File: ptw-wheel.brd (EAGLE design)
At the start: 54 x 45 mm, 4 parts

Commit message: Replace GND to N$1 ?
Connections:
- net GND renamed N$1
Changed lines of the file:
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@@
 </elements>
 <signals>
-<signal name="GND">
-<contactref element="U$1" pad="GND"/>
-<contactref element="USB1" pad="GND"/>
-<contactref element="USB1" pad="SHIELD1"/>
-<contactref element="USB1" pad="SHIELD2"/>
-<contactref element="U$1" pad="GND@1"/>
-<contactref element="JP1" pad="3"/>
-<contactref element="ARDUINO_NANO1" pad="19"/>
-<contactref element="ARDUINO_NANO1" pad="14"/>
-<contactref element="U$1" pad="GND@3"/>
-<contactref element="U$1" pad="GND@2"/>
-<polygon width="1" layer="16">
-<vertex x="1" y="44"/>
-<vertex x="53" y="44"/>
-<vertex x="53" y="1"/>
-<vertex x="1" y="1"/>
-</polygon>
-<polygon width="1" layer="1">
-<vertex x="1" y="44"/>
-<vertex x="53" y="44"/>
-<vertex x="53" y="1"/>
-<vertex x="1" y="1"/>
-</polygon>
-</signal>
 <signal name="+3V">
 <contactref element="U$1" pad="+3V"/>
@@
 <wire x1="38.8" y1="29.8" x2="39" y2="30" width="1" layer="1"/>
 </signal>
+<signal name="N$1">
+<contactref element="U$1" pad="GND"/>
+<contactref element="USB1" pad="GND"/>
+<contactref element="USB1" pad="SHIELD1"/>
+<contactref element="USB1" pad="SHIELD2"/>
+<contactref element="U$1" pad="GND@1"/>
+<contactref element="JP1" pad="3"/>
+<contactref element="ARDUINO_NANO1" pad="19"/>
+<contactref element="ARDUINO_NANO1" pad="14"/>
+<contactref element="U$1" pad="GND@3"/>
+<contactref element="U$1" pad="GND@2"/>
+<polygon width="1" layer="16">
+<vertex x="1" y="44"/>
+<vertex x="53" y="44"/>
+<vertex x="53" y="1"/>
+<vertex x="1" y="1"/>
+</polygon>
+<polygon width="1" layer="1">
+<vertex x="1" y="44"/>
+<vertex x="53" y="44"/>
+<vertex x="53" y="1"/>
+<vertex x="1" y="1"/>
+</polygon>
+</signal>
 </signals>

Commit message: Export NetScript file and import it on the brd file
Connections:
- net N$1 renamed GND
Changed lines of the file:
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@@
 <wire x1="38.8" y1="29.8" x2="39" y2="30" width="1" layer="1"/>
 </signal>
-<signal name="N$1">
+<signal name="GND">
 <contactref element="U$1" pad="GND"/>
 <contactref element="USB1" pad="GND"/>
@@
 <vertex x="1" y="1"/>
 </polygon>
+<wire x1="12.7" y1="33.02" x2="42.54" y2="33" width="0" layer="19" extent="1-16"/>
+<wire x1="42.54" y1="33" x2="50.8" y2="11.16" width="0" layer="19" extent="1-16"/>
+<wire x1="50.8" y1="11.16" x2="50.8" y2="26.4" width="0" layer="19" extent="1-16"/>
+<wire x1="50.8" y1="26.4" x2="2.54" y2="11.16" width="0" layer="19" extent="1-16"/>
+<wire x1="2.54" y1="11.16" x2="41.2" y2="9.66" width="0" layer="19" extent="1-16"/>
+<wire x1="41.2" y1="9.66" x2="43.7" y2="4.01" width="0" layer="19" extent="1-16"/>
+<wire x1="43.7" y1="4.01" x2="36.3" y2="4.01" width="0" layer="19" extent="1-16"/>
+<wire x1="27.94" y1="38.1" x2="2.54" y2="31.48" width="0" layer="19" extent="1-16"/>
 </signal>
 </signals>

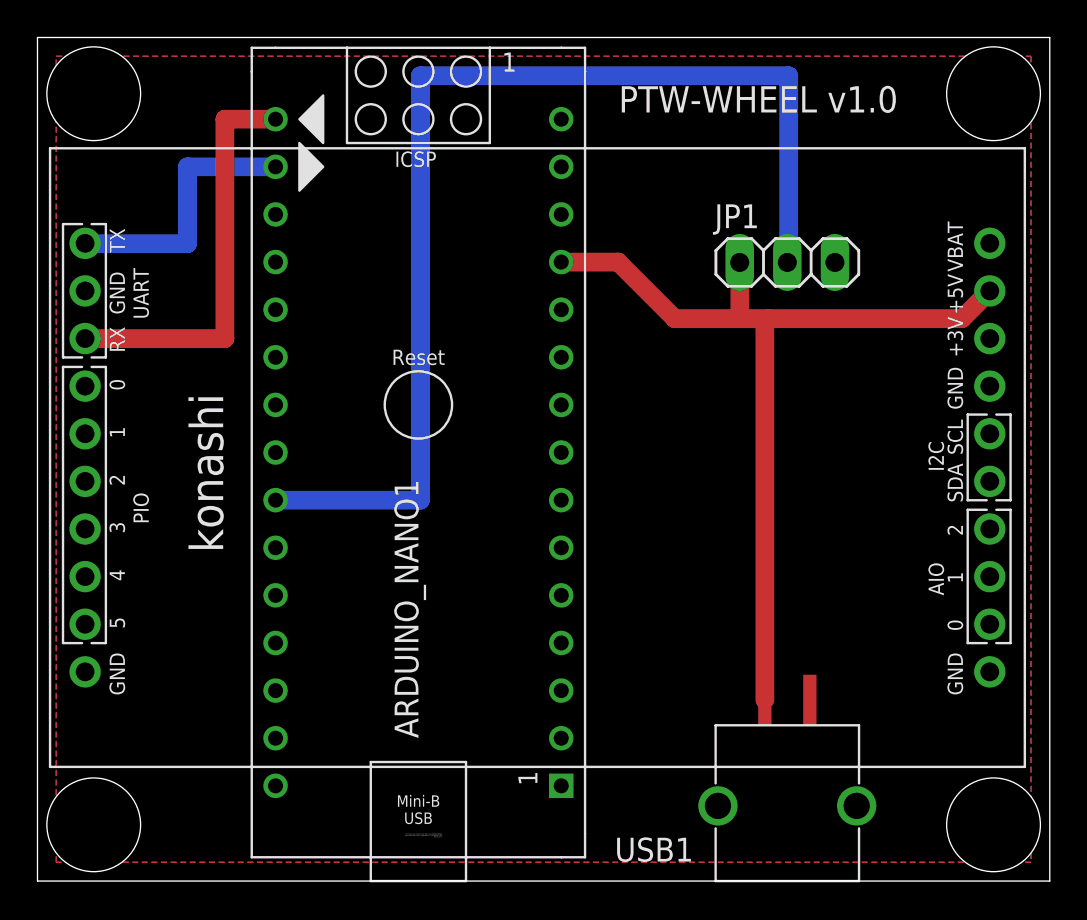
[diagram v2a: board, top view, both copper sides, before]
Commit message: Move konashi position
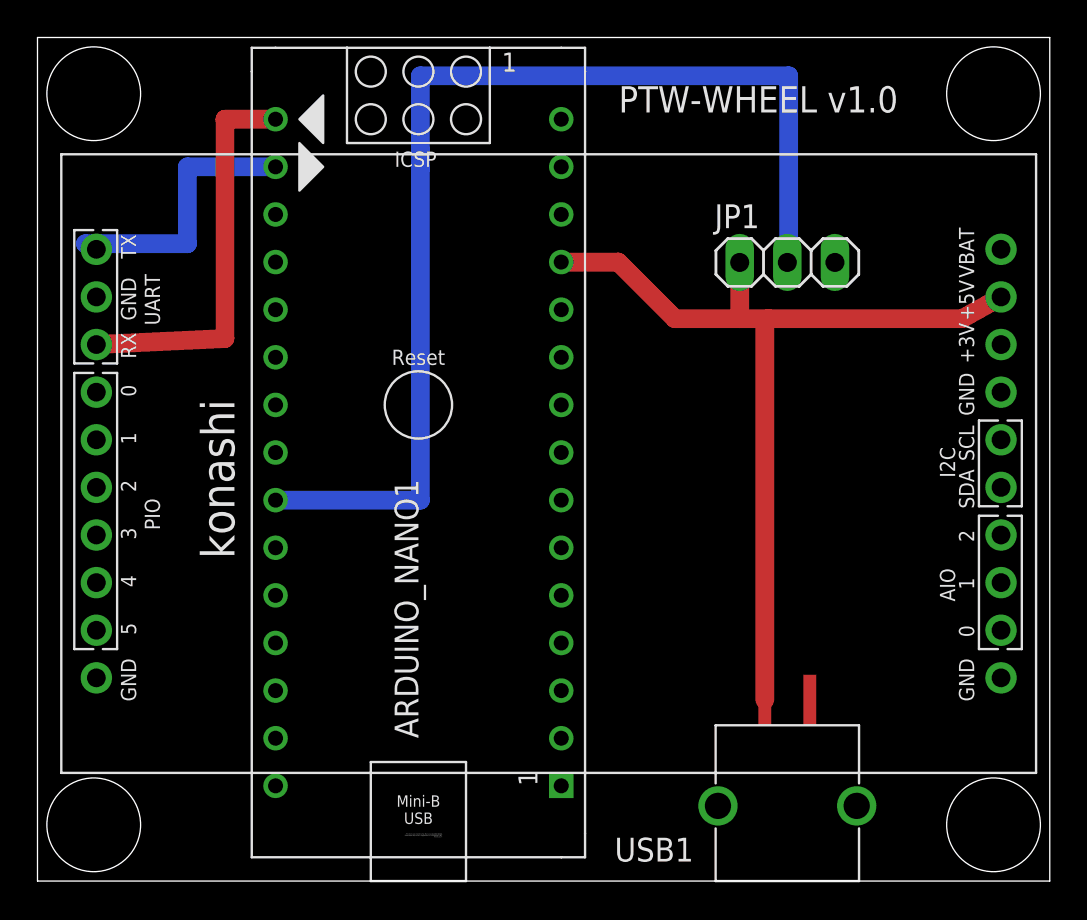
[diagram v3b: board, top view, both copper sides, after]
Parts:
- moved U$1 0.68 mm to (26.0, 21.0)
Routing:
- net N$4: track 14.3 -> 14.9 mm
- net N$5: track 21.9 -> 21.3 mm
- removed copper zone on layer 1, net GND
- removed copper zone on layer 16, net GND
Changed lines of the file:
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@@
 <attribute name="VALUE" x="36.19" y="29.825" size="1.27" layer="27"/>
 </element>
-<element name="U$1" library="konashiv2-withoud_drill_hole" package="KONASHI" value="KONASHI2.0" x="25.4" y="21.32" smashed="yes" rot="R90"/>
+<element name="U$1" library="konashiv2-withoud_drill_hole" package="KONASHI" value="KONASHI2.0" x="26" y="21" smashed="yes" rot="R90"/>
 <element name="USB1" library="usbcon" package="USBCON" value="USBCON" x="40" y="8.31" smashed="yes" rot="R180">
 <attribute name="NAME" x="35" y="2.31" size="1.27" layer="25" rot="R180"/>
@@
 <wire x1="8" y1="38.1" x2="8" y2="34" width="1" layer="16"/>
 <wire x1="8" y1="34" x2="2.56" y2="34" width="1" layer="16"/>
-<wire x1="2.56" y1="34" x2="2.54" y2="34.02" width="1" layer="16"/>
+<wire x1="2.56" y1="34" x2="3.14" y2="33.7" width="1" layer="16"/>
 </signal>
 <signal name="N$5">
 <contactref element="U$1" pad="RX"/>
 <contactref element="ARDUINO_NANO1" pad="16"/>
-<wire x1="2.54" y1="28.94" x2="10" y2="28.94" width="1" layer="1"/>
+<wire x1="3.14" y1="28.62" x2="10" y2="28.94" width="1" layer="1"/>
 <wire x1="10" y1="28.94" x2="10" y2="40.629840625" width="1" layer="1"/>
 <wire x1="10.010159375" y1="40.64" x2="10" y2="40.629840625" width="1" layer="1"/>
@@
 <wire x1="37.462459375" y1="30" x2="39" y2="30" width="1" layer="1"/>
 <wire x1="39" y1="30" x2="49.32" y2="30" width="1" layer="1"/>
-<wire x1="49.32" y1="30" x2="50.8" y2="31.48" width="1" layer="1"/>
+<wire x1="49.32" y1="30" x2="51.4" y2="31.16" width="1" layer="1"/>
 <wire x1="38.8" y1="9.66" x2="38.8" y2="29.8" width="1" layer="1"/>
 <wire x1="38.8" y1="29.8" x2="39" y2="30" width="1" layer="1"/>
@@
 <contactref element="U$1" pad="GND@3"/>
 <contactref element="U$1" pad="GND@2"/>
-<polygon width="1" layer="16">
-<vertex x="1" y="44"/>
-<vertex x="53" y="44"/>
-<vertex x="53" y="1"/>
-<vertex x="1" y="1"/>
-</polygon>
-<polygon width="1" layer="1">
-<vertex x="1" y="44"/>
-<vertex x="53" y="44"/>
-<vertex x="53" y="1"/>
-<vertex x="1" y="1"/>
-</polygon>
 <wire x1="12.7" y1="33.02" x2="42.54" y2="33" width="0" layer="19" extent="1-16"/>
-<wire x1="42.54" y1="33" x2="50.8" y2="11.16" width="0" layer="19" extent="1-16"/>
-<wire x1="50.8" y1="11.16" x2="50.8" y2="26.4" width="0" layer="19" extent="1-16"/>
-<wire x1="50.8" y1="26.4" x2="2.54" y2="11.16" width="0" layer="19" extent="1-16"/>
-<wire x1="2.54" y1="11.16" x2="41.2" y2="9.66" width="0" layer="19" extent="1-16"/>
+<wire x1="42.54" y1="33" x2="51.4" y2="10.84" width="0" layer="19" extent="1-16"/>
+<wire x1="51.4" y1="10.84" x2="51.4" y2="26.08" width="0" layer="19" extent="1-16"/>
+<wire x1="51.4" y1="26.08" x2="3.14" y2="10.84" width="0" layer="19" extent="1-16"/>
+<wire x1="3.14" y1="10.84" x2="41.2" y2="9.66" width="0" layer="19" extent="1-16"/>
 <wire x1="41.2" y1="9.66" x2="43.7" y2="4.01" width="0" layer="19" extent="1-16"/>
 <wire x1="43.7" y1="4.01" x2="36.3" y2="4.01" width="0" layer="19" extent="1-16"/>
-<wire x1="27.94" y1="38.1" x2="2.54" y2="31.48" width="0" layer="19" extent="1-16"/>
+<wire x1="27.94" y1="38.1" x2="3.14" y2="31.16" width="0" layer="19" extent="1-16"/>
 </signal>
 </signals>
